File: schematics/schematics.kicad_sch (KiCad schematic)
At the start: 16 parts, among them U10 74AHC1G00, U7 4072, U8 4077

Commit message: More tests
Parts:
- removed C1, C2, C4, C5, C6: C_Small, Capacitor_SMD:C_1206_3216Metric, symbol Device:C_Small
- removed U10: 74AHC1G00, symbol 74xGxx:74AHC1G00
- removed U7: 4072, symbol 4xxx:4072
- removed U8: 4077, symbol 4xxx:4077
- added NAND1: SN74LS00NE4, DIP794W53P254L1930H508Q14N, symbol SN74LS00NE4:SN74LS00NE4
- added OR_1: CD4072BE, DIP794W53P254L1930H508Q14N, symbol CD4072BE:CD4072BE
- added XNOR1: CD4077BE, DIP794W53P254L1930H508Q14N, symbol CD4077BE:CD4077BE
- added ~{NMI}_SW1: SW_Push, Button_Switch_THT:SW_Tactile_SKHH_Angled, symbol Switch:SW_Push
- ADDR_1_LS1, ADDR_2_LS1, DATA_LS1, PICO_IN_LS1, PICO_OUT_LS1: footprint Package_SO:SO-20_5.3x12.6mm_P1.27mm -> DIP794W53P254L2540H508Q20N; symbol 74xx:74LS245 -> SN74LVC245ANE4:SN74LVC245ANE4; Height (none) -> 5.08; Manufacturer_Name (none) -> Texas Instruments; Manufacturer_Part_Number (none) -> SN74LVC245ANE4; Mouser Part Number (none) -> 595-SN74LVC245ANE4; Mouser Price/Stock (none) -> https://www.mouser.co.uk/ProductDetail/Texas-Instruments/SN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
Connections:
- net ~{ZX_ROMCS} is gone; now on net ~{ZXROMCS}: Z1.B25 (~{ROMCS})
- net +3V3: now also NAND1.14 (VCC), OR_1.14 (VDD), XNOR1.14 (VDD)
- net D3: now also DATA_LS1.15 (B4); no longer DATA_LS1.14 (B4)
- net D4: now also DATA_LS1.14 (B5); no longer DATA_LS1.12 (B6)
- net D5: now also DATA_LS1.13 (B6); no longer DATA_LS1.15 (B3)
- net D6: now also DATA_LS1.12 (B7); no longer DATA_LS1.13 (B5)
- net GND: now also ADDR_1_LS1.19 (~{OE}), ADDR_2_LS1.19 (~{OE}), PICO_IN_LS1.19 (~{OE}), PICO_OUT_LS1.19 (~{OE}), NAND1.7 (GND), OR_1.7 (VSS), XNOR1.7 (VSS), ~{NMI}_SW1.2; no longer RP2040-PICO30.42 (GND)
- net ZXA14: now also OR_1.3 (B)
- net ZXA15: now also OR_1.2 (A)
- net ZXD3: now also DATA_LS1.5 (A4); no longer DATA_LS1.6 (A4)
- net ZXD4: now also DATA_LS1.6 (A5); no longer DATA_LS1.8 (A6)
- net ZXD5: now also DATA_LS1.7 (A6); no longer DATA_LS1.5 (A3)
- net ZXD6: now also DATA_LS1.8 (A7); no longer DATA_LS1.7 (A5)
- net ZX_NO_INT: now also NAND1.3 (1Y)
- net ~{CP/M}: now also PICO_IN_LS1.14 (B5); no longer PICO_IN_LS1.15 (B3)
- net ~{OE}: now also NAND1.4 (2A); no longer ADDR_1_LS1.19 (CE), ADDR_2_LS1.19 (CE), DATA_LS1.19 (CE), PICO_IN_LS1.19 (CE), PICO_OUT_LS1.19 (CE)
- net ~{RD}: now also DATA_LS1.1 (DIR)
- net ~{WAIT}: no longer PICO_OUT_LS1.3 (A1)
- net ~{ZXCP/M}: now also PICO_IN_LS1.6 (A5); no longer PICO_IN_LS1.5 (A3)
- net ~{ZXIORQ}: now also NAND1.2 (1B), XNOR1.2 (B)
- net ~{ZXM1}: now also PICO_IN_LS1.5 (A4), NAND1.1 (1A)
- net ~{ZXMREQ}: now also XNOR1.1 (A)
- net ~{ZXPI_EN}: now also NAND1.5 (2B), OR_1.1 (J=A+B+C+D)
- net ~{ZXRD}: now also XNOR1.5 (C); no longer DATA_LS1.1 (A->B)
- net ~{ZXWAIT}: now also PICO_OUT_LS1.3 (A2)
- net ~{ZX_M_IO_REQ}: now also OR_1.4 (C), XNOR1.3 (J)
- net ~{ZXNMI}: now reaches Z1.A14 (~{NMI})
- net ~{ZXNMI}: now also ~{NMI}_SW1.1
- net SPARE_1 renamed ~{M1}
- net ~{M1}: now also PICO_IN_LS1.15 (B4)
- removed net SWDCLK: RP2040-PICO30.41 (SWCLK)
- removed net SWDIO: RP2040-PICO30.43 (SWDIO)
- net ~{ZXIORQGE}: no longer names the net of Z1.B13 (~{IORQGE})
- net ~{ZXROMCS2}: no longer names the net of Z1.B15 (~{ROMCS2})
- new net ~{DATA_OE}: DATA_LS1.19 (~{OE}), NAND1.6 (2Y)
- new net ~{ZXWR}: XNOR1.6 (D)
- new net ~{ZX_RD_WR}: OR_1.5 (D), XNOR1.4 (K)
- no-connect marks 29 -> 62
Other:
- note added: "~{ZXPI_EN} logic breakdown: - ZXA15 || ZXA14 - both must be low (only first 16k) - !(ZXMREQ ^ ZXIOREQ) - only one is low - !(ZXRD ^ ZXWR) - only one is low - !(ZXM1 & ZXIOREQ) - not an interrupt"
- note added: "~{ZXPI_EN} logic. ~{ZXPI_EN} is low when: ZXA15 || ZXA14 || !(ZXMREQ ^ ZXIOREQ) || !(ZXRD ^ ZXWR) || !(ZXM1 & ZXIOREQ)"
- note removed: "~{ZXPI_EN} logic breakdown: - ZXA15 || ZXA14 - both must be low (only first 16k) - !(ZXMREQ ^ ZXIOREQ) - only one is low - !(ZXM1 & ZXIOREQ) - not an interrupt"
- note removed: "~{ZXPI_EN} logic. ~{ZXPI_EN} is low when: ZXA15 || ZXA14 || !(ZXMREQ ^ ZXIOREQ) || !(ZXM1 & ZXIOREQ)"
- title: Interface 3.14 -> IFp

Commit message: Fix schematics
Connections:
- net ~{DATA_OE}: no longer DATA_LS1.19 (~{OE})
- net ~{OE}: now also DATA_LS1.19 (~{OE})
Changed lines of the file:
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@@
+		)
+	)
+	(label "unused"
+		(at 139.7 180.34 0)
+		(fields_autoplaced yes)
+		(effects
+			(font
+				(size 1.27 1.27)
+			)
+			(justify left bottom)
 		)
 	)
@@
 		)
 	)
-	(global_label "~{DATA_OE}"
+	(global_label "~{OE}"
 		(shape input)
 		(at 58.42 114.3 0)
@@
 		)
 		(property "Intersheetrefs" "${INTERSHEET_REFS}"
-			(at 69.2671 114.3 0)
-			(effects
-				(font
+			(at 63.8847 114.3 0)
+			(effects
+				(font

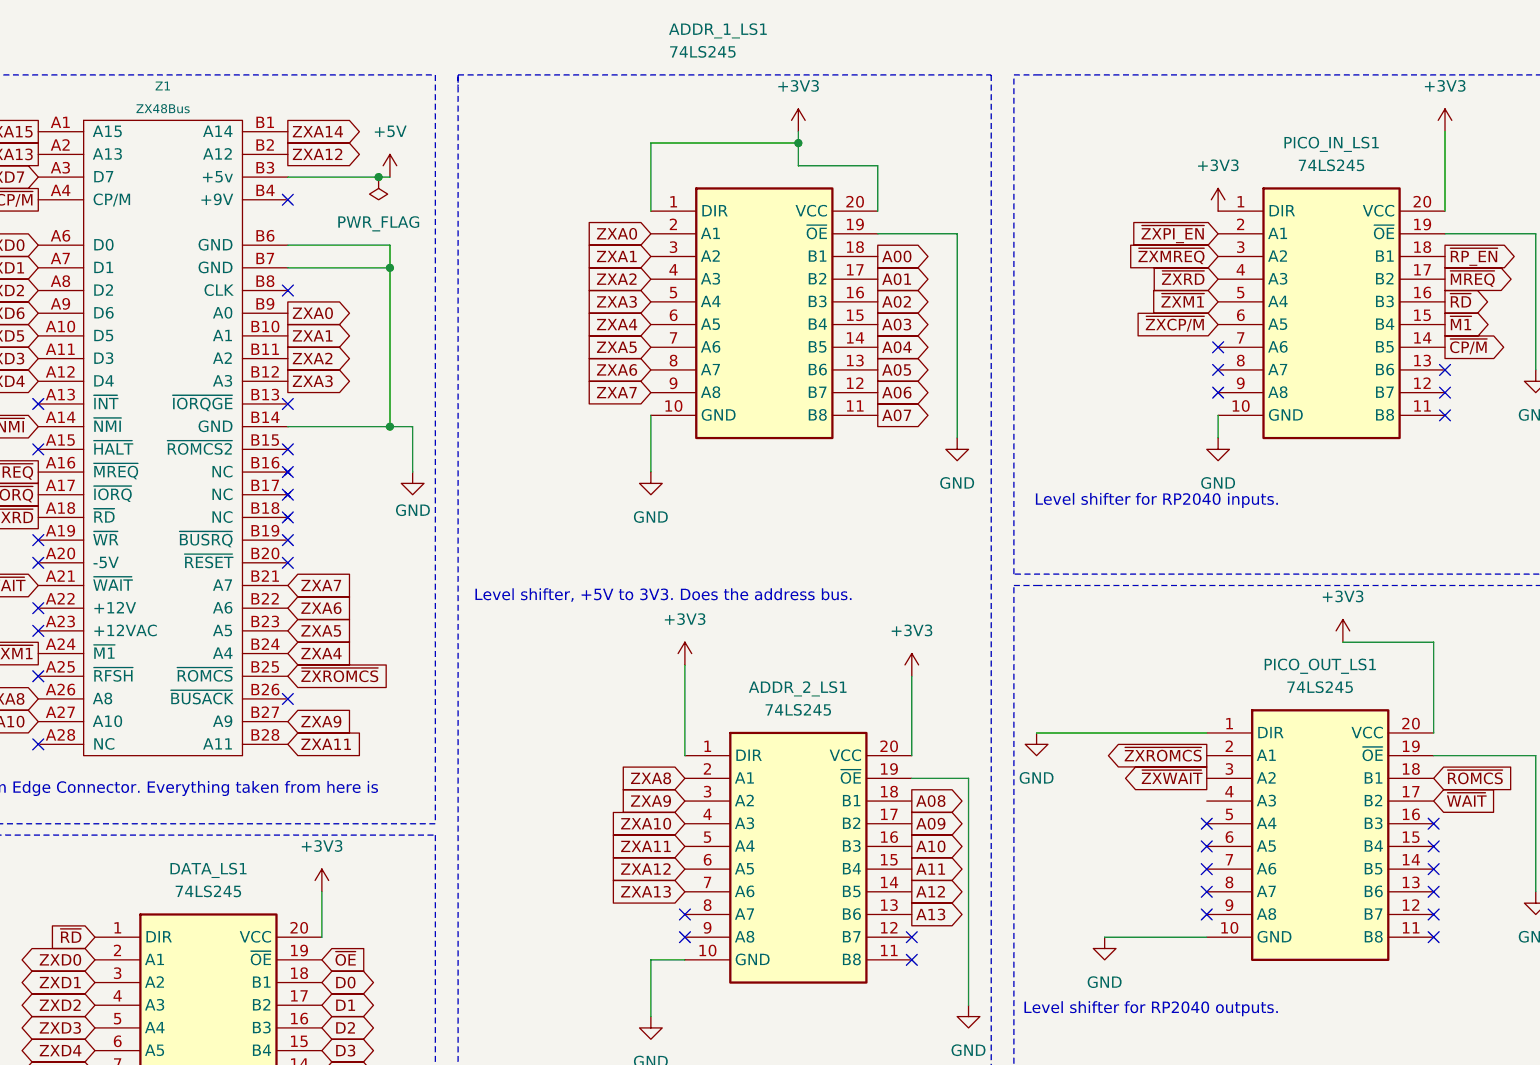
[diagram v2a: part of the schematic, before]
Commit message: Fix 74xx245 naming
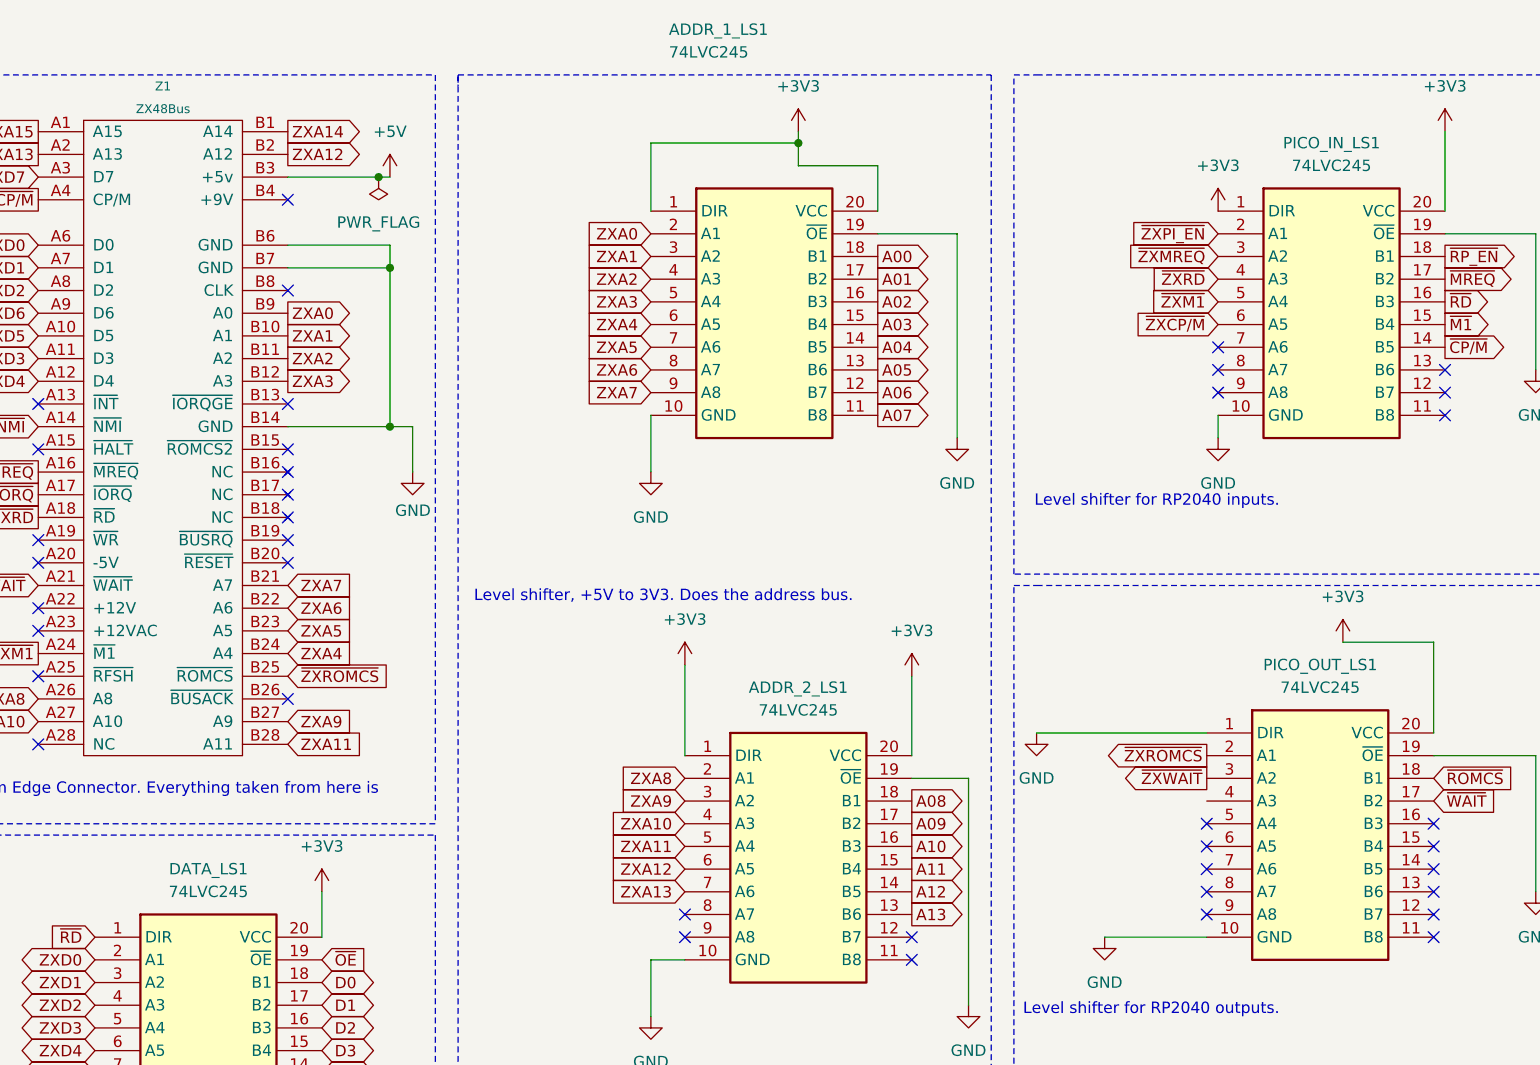
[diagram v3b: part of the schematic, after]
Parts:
- ADDR_1_LS1, ADDR_2_LS1, DATA_LS1, PICO_IN_LS1, PICO_OUT_LS1: value 74LS245 -> 74LVC245
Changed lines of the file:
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@@
 			)
 		)
-		(property "Value" "74LS245"
+		(property "Value" "74LVC245"
 			(at 45.72 106.68 0)
 			(effects
@@
 			)
 		)
-		(property "Value" "74LS245"
+		(property "Value" "74LVC245"
 			(at 171.45 25.4 0)
 			(effects
@@
 			)
 		)
-		(property "Value" "74LS245"
+		(property "Value" "74LVC245"
 			(at 170.18 83.82 0)
 			(effects
@@
 			)
 		)
-		(property "Value" "74LS245"
+		(property "Value" "74LVC245"
 			(at 97.2694 12.7 0)
 			(effects
@@
 			)
 		)
-		(property "Value" "74LS245"
+		(property "Value" "74LVC245"
 			(at 111.76 86.36 0)
 			(effects

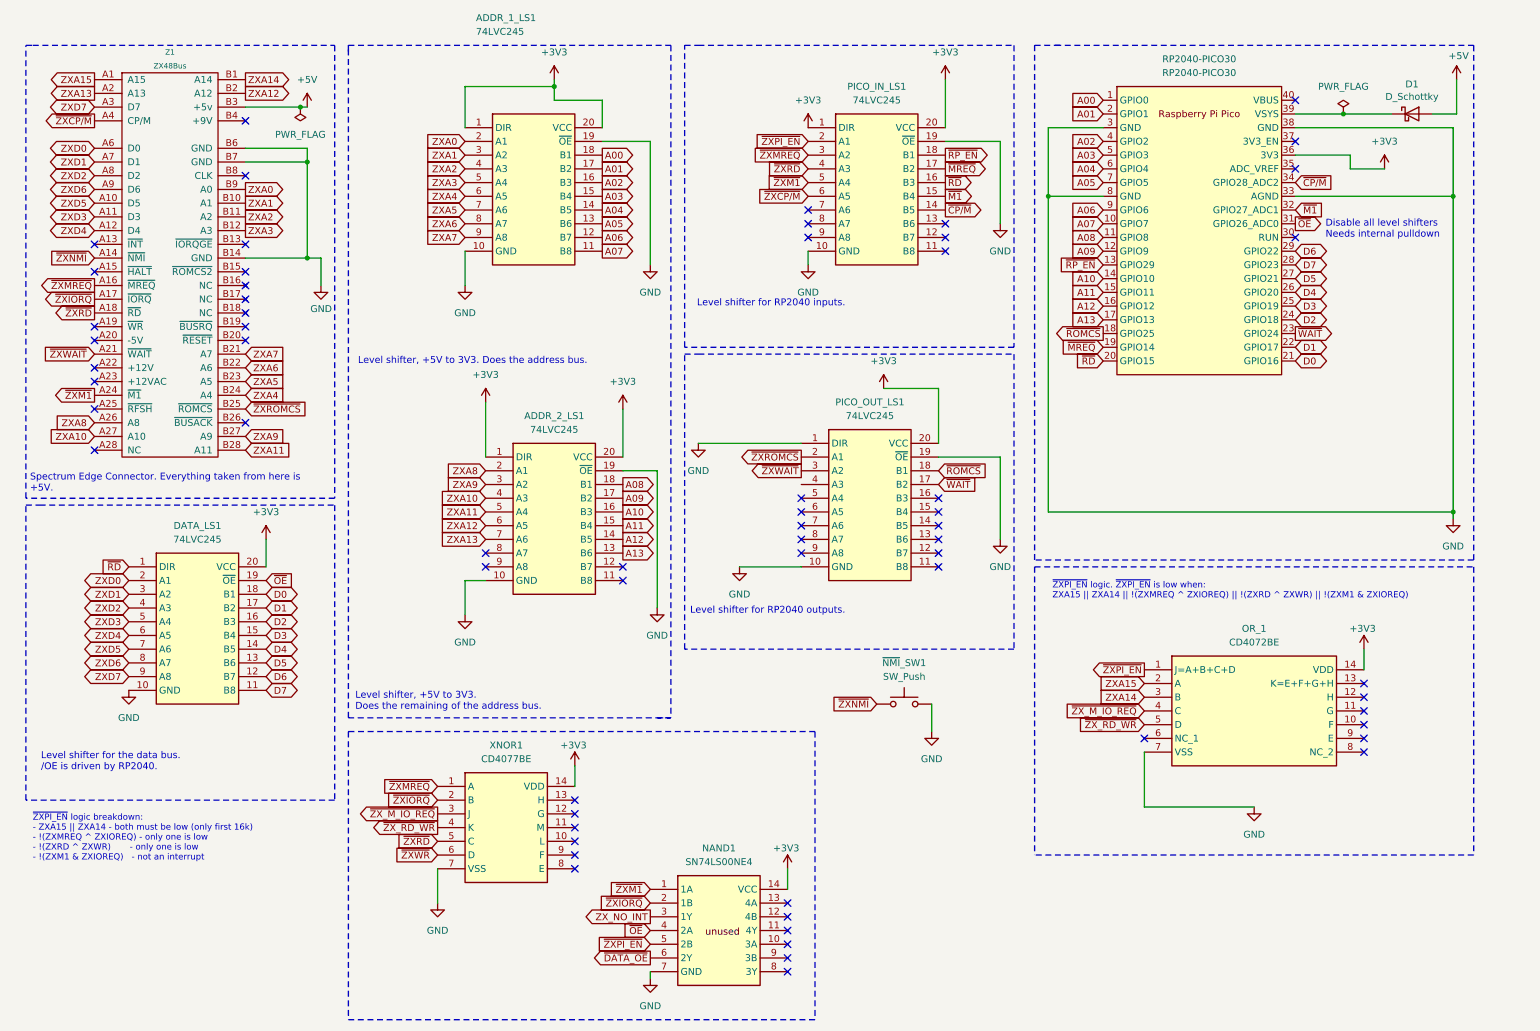
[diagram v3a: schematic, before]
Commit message: Switched to olimex pico2 xxl
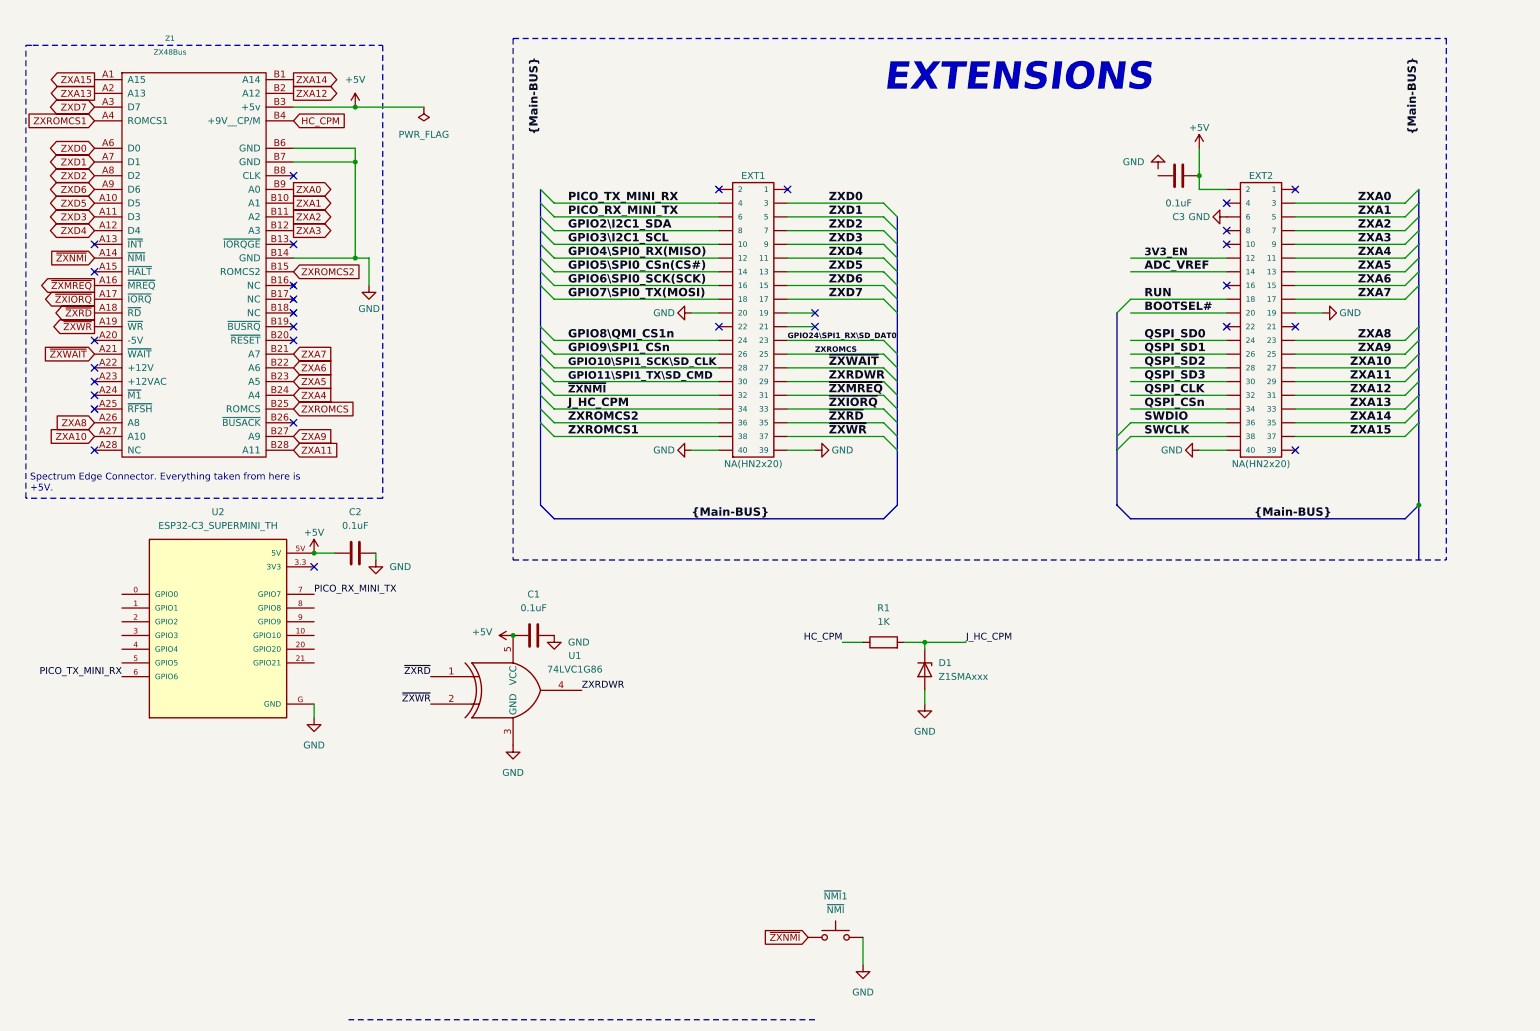
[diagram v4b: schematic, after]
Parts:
- removed ADDR_1_LS1, ADDR_2_LS1, DATA_LS1, PICO_IN_LS1, PICO_OUT_LS1: 74LVC245, DIP794W53P254L2540H508Q20N, symbol SN74LVC245ANE4:SN74LVC245ANE4
- removed D1: D_Schottky, Diode_SMD:D_1206_3216Metric_Pad1.42x1.75mm_HandSolder, symbol Device:D_Schottky
- removed NAND1: SN74LS00NE4, DIP794W53P254L1930H508Q14N, symbol SN74LS00NE4:SN74LS00NE4
- removed OR_1: CD4072BE, DIP794W53P254L1930H508Q14N, symbol CD4072BE:CD4072BE
- removed RP2040-PICO30: RP2040-PICO30, pico-foot:RPi_Pico_SMD_TH, symbol pico-sym:Pico
- removed XNOR1: CD4077BE, DIP794W53P254L1930H508Q14N, symbol CD4077BE:CD4077BE
- added C1, C2, C3: 0.1uF, Capacitor_SMD:C_1210_3225Metric, symbol Device:C
- added D1: Z1SMAxxx, Diode_SMD:D_SMA, symbol Diode:Z1SMAxxx
- added EXT1, EXT2: NA(HN2x20), OLIMEX_Connectors-FP:HN2x20, symbol OLIMEX_Connectors:BH40S
- added R1: 1K, Resistor_SMD:R_0805_2012Metric, symbol Device:R
- added U1: 74LVC1G86, Package_TO_SOT_SMD:SOT-353_SC-70-5, symbol 74xGxx:74LVC1G86
- added U2: ESP32-C3_SUPERMINI_TH, ESP32-C_SUPERMINI:MODULE_ESP32-C3_SUPERMINI_TH, symbol ESP32-C3_SUPERMINI_TH:ESP32-C3_SUPERMINI_TH
- Z1: footprint zxbus:ZX_Bus_Pin_Header -> zxbus:ZX_Bus_Edge_Connector
- ~{NMI}1: renamed from ~{NMI}_SW1; value SW_Push -> ~{NMI}
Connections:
- net +5V: now also C1.1, C2.1, C3.1, EXT2.2, U1.5 (VCC), U2.5V
- net GND: now also C1.2, C2.2, D1.2 (A), EXT1.20, EXT1.39, EXT1.40, EXT2.19, EXT2.40, EXT2.6, U1.3 (GND), U2.G (GND)
- net ZXA0: now also EXT2.3
- net ZXA1: now also EXT2.5
- net ZXA10: now also EXT2.27
- net ZXA11: now also EXT2.29
- net ZXA12: now also EXT2.31
- net ZXA13: now also EXT2.33
- net ZXA14: now also EXT2.35
- net ZXA15: now also EXT2.37
- net ZXA2: now also EXT2.7
- net ZXA3: now also EXT2.9
- net ZXA4: now also EXT2.11
- net ZXA5: now also EXT2.13
- net ZXA6: now also EXT2.15
- net ZXA7: now also EXT2.17
- net ZXA8: now also EXT2.23
- net ZXA9: now also EXT2.25
- net ZXD0: now also EXT1.3
- net ZXD1: now also EXT1.5
- net ZXD2: now also EXT1.7
- net ZXD3: now also EXT1.9
- net ZXD4: now also EXT1.11
- net ZXD5: now also EXT1.13
- net ZXD6: now also EXT1.15
- net ZXD7: now also EXT1.17
- net ~{ZXIORQ}: now also EXT1.33
- net ~{ZXMREQ}: now also EXT1.31
- net ~{ZXNMI}: now also EXT1.32
- net ~{ZXRD}: now also EXT1.35, U1.1
- net ~{ZXWAIT}: now also EXT1.27
- net ~{ZXWR}: now also Z1.A19 (~{WR}), EXT1.37, U1.2
- net ZXROMCS2: now reaches Z1.B15 (ROMCS2)
- net ZXROMCS2: now also EXT1.36
- net HC_CPM: now reaches Z1.B4 (+9V__CP/M)
- net HC_CPM: now also R1.1
- net ~{ZXCP/M} renamed ZXROMCS1
- net ZXROMCS1: now also EXT1.38
- net ~{ZXM1}: no longer names the net of Z1.A24 (~{M1})
- net ~{ZXROMCS} renamed ZXROMCS
- net ZXROMCS: now also EXT1.25
- new net 3V3_EN: EXT2.12
- new net ADC_VREF: EXT2.14
- new net BOOTSEL#: EXT2.20
- new net GPIO10\SPI1_SCK\SD_CLK: EXT1.28
- new net GPIO11\SPI1_TX\SD_CMD: EXT1.30
- new net GPIO24\SPI1_RX\SD_DAT0: EXT1.23
- new net GPIO2\I2C1_SDA: EXT1.8
- new net GPIO3\I2C1_SCL: EXT1.10
- new net GPIO4\SPI0_RX(MISO): EXT1.12
- new net GPIO5\SPI0_CSn(CS#): EXT1.14
- new net GPIO6\SPI0_SCK(SCK): EXT1.16
- new net GPIO7\SPI0_TX(MOSI): EXT1.18
- new net GPIO8\QMI_CS1n: EXT1.24
- new net GPIO9\SPI1_CSn: EXT1.26
- new net J_HC_CPM: D1.1 (K), EXT1.34, R1.2
- new net PICO_RX_MINI_TX: EXT1.6, U2.7 (GPIO7)
- new net PICO_TX_MINI_RX: EXT1.4, U2.6 (GPIO6)
- new net QSPI_CLK: EXT2.32
- new net QSPI_CSn: EXT2.34
- new net QSPI_SD0: EXT2.24
- new net QSPI_SD1: EXT2.26
- new net QSPI_SD2: EXT2.28
- new net QSPI_SD3: EXT2.30
- new net RUN: EXT2.18
- new net SWCLK: EXT2.38
- new net SWDIO: EXT2.36
- new net ZXRDWR: EXT1.29, U1.4
- no-connect marks 62 -> 30
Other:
- note added: "EXTENSIONS"
- note removed: "Disable all level shifters Needs internal pulldown"
- note removed: "Level shifter for RP2040 inputs."
- note removed: "Level shifter for RP2040 outputs."
- note removed: "Level shifter for the data bus. /OE is driven by RP2040."
- note removed: "Level shifter, +5V to 3V3. Does the address bus."
- note removed: "Level shifter, +5V to 3V3. Does the remaining of the address bus."
- note removed: "~{ZXPI_EN} logic breakdown: - ZXA15 || ZXA14 - both must be low (only first 16k) - !(ZXMREQ ^ ZXIOREQ) - only one is low - !(ZXRD ^ ZXWR) - only one is low - !(ZXM1 & ZXIOREQ) - not an interrupt"
- note removed: "~{ZXPI_EN} logic. ~{ZXPI_EN} is low when: ZXA15 || ZXA14 || !(ZXMREQ ^ ZXIOREQ) || !(ZXRD ^ ZXWR) || !(ZXM1 & ZXIOREQ)"
- moved on the sheet: Z1, ~{NMI}1
